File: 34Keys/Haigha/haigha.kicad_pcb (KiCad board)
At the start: 2 copper layers, 114.4 x 88.3 mm, 20 parts, among them J1 MJ-4PP-9, SW10 SW_PUSH, SW11 SW_PUSH, SW12 SW_PUSH, SW14 SW_PUSH, SW15 SW_PUSH, SW16 SW_PUSH, SW17 SW_PUSH, SW18 SW_PUSH, SW2 SW_PUSH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

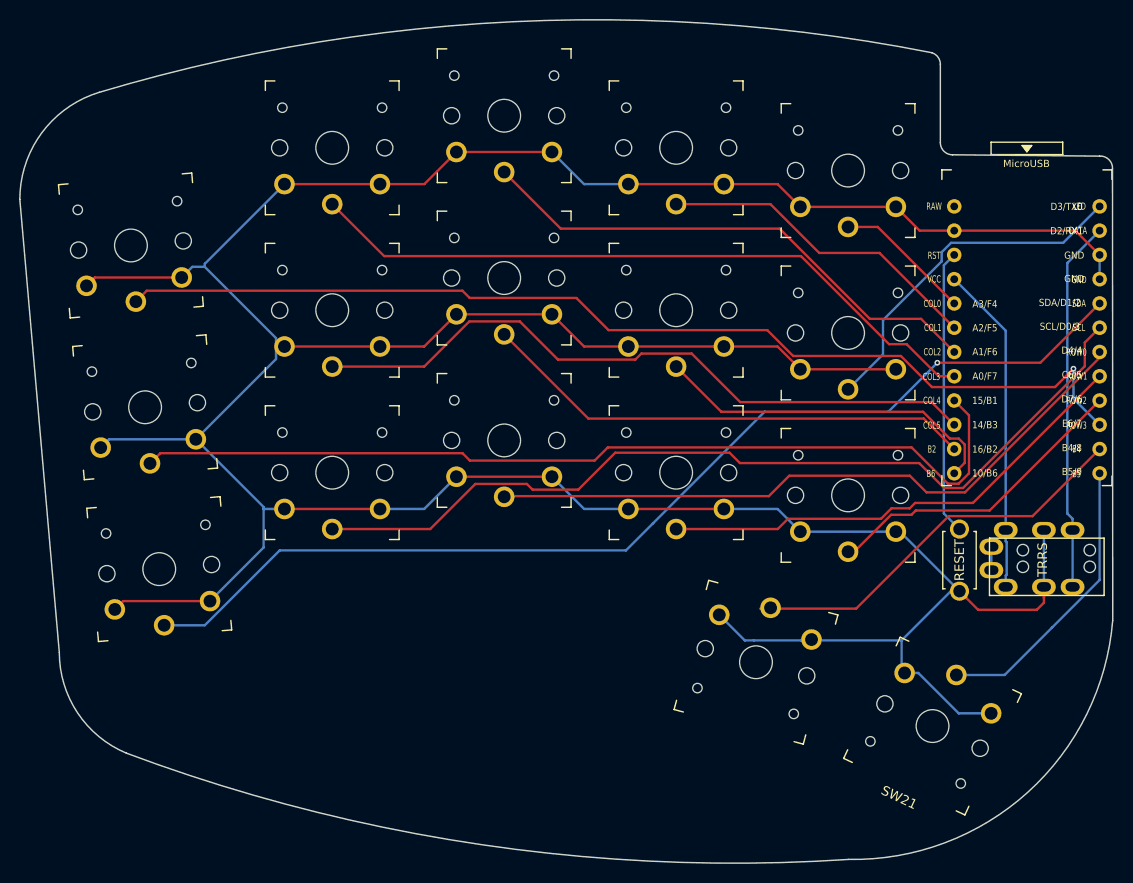
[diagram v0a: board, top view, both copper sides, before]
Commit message: Re route haigha tracks
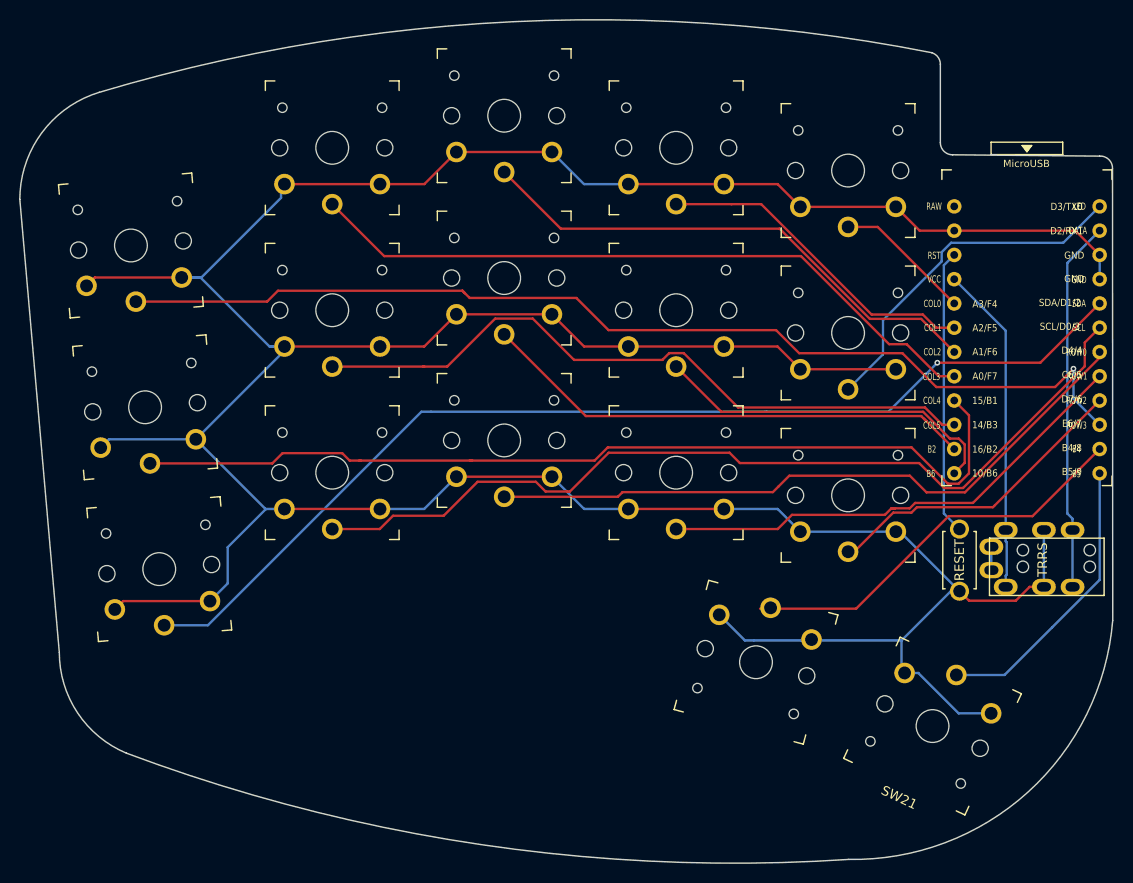
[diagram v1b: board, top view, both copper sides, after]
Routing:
- net GND: track 396.9 -> 398.5 mm
